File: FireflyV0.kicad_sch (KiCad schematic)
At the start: 18 parts, among them J1 USB4125-GF-A-0190, J2 USB4125-GF-A-0190, J3 USB4125-GF-A-0190, J4 Conn_01x04, J5 Conn_01x03, U1 PEC12R-4215F-S0024, U2 Pico

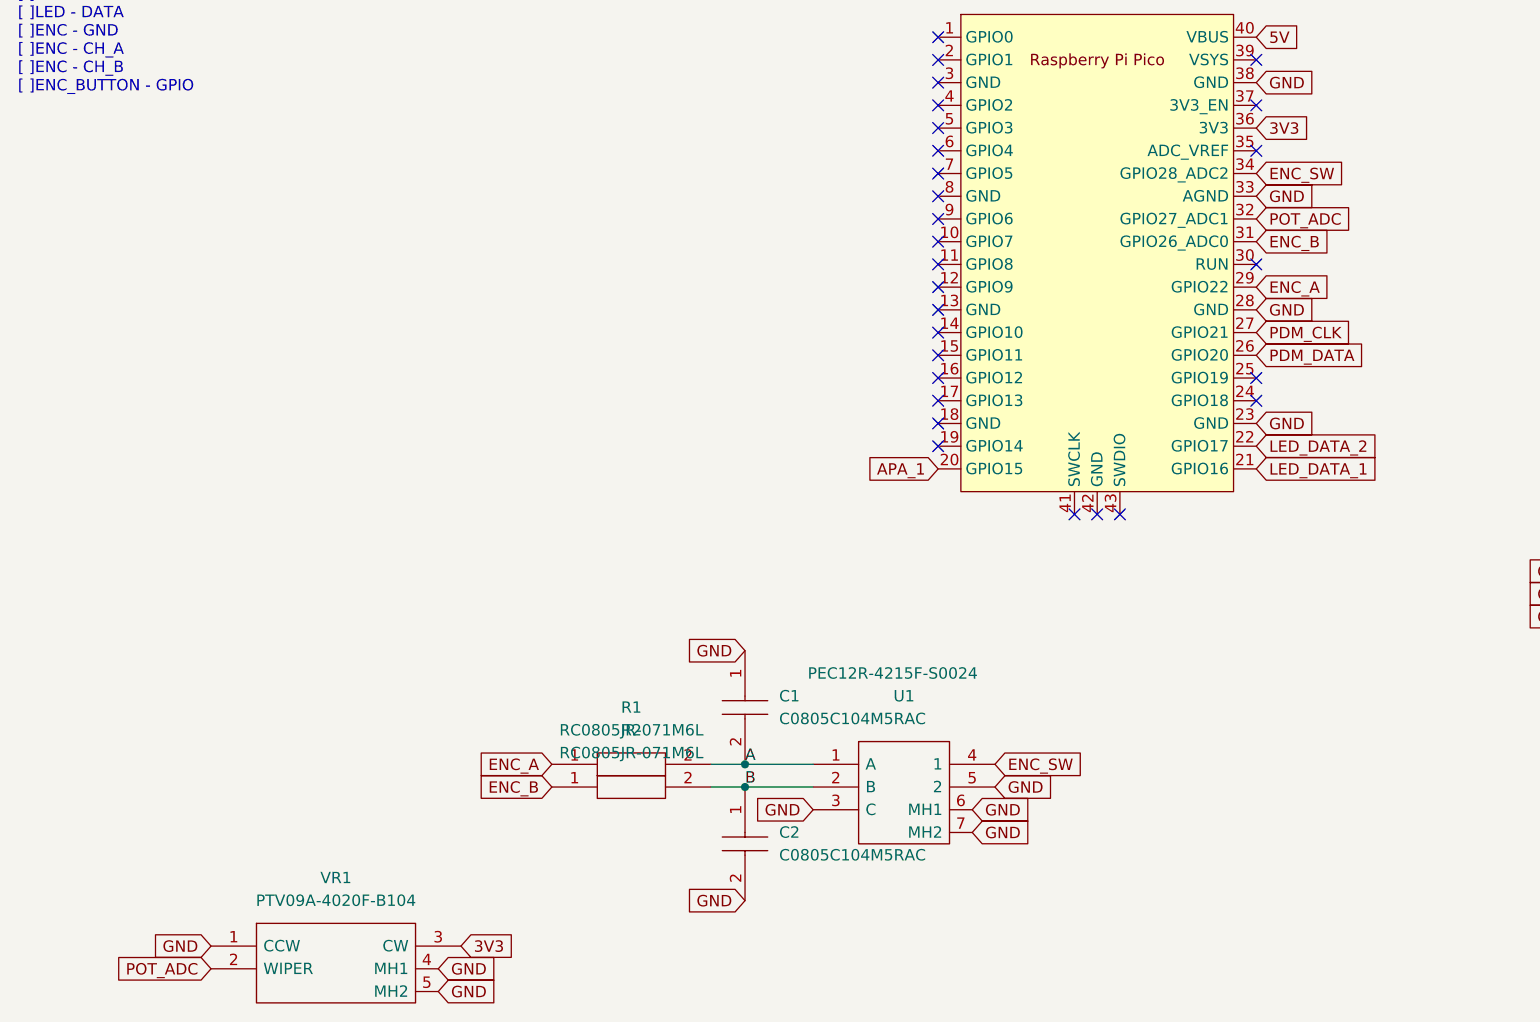
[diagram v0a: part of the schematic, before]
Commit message: Adding puttons
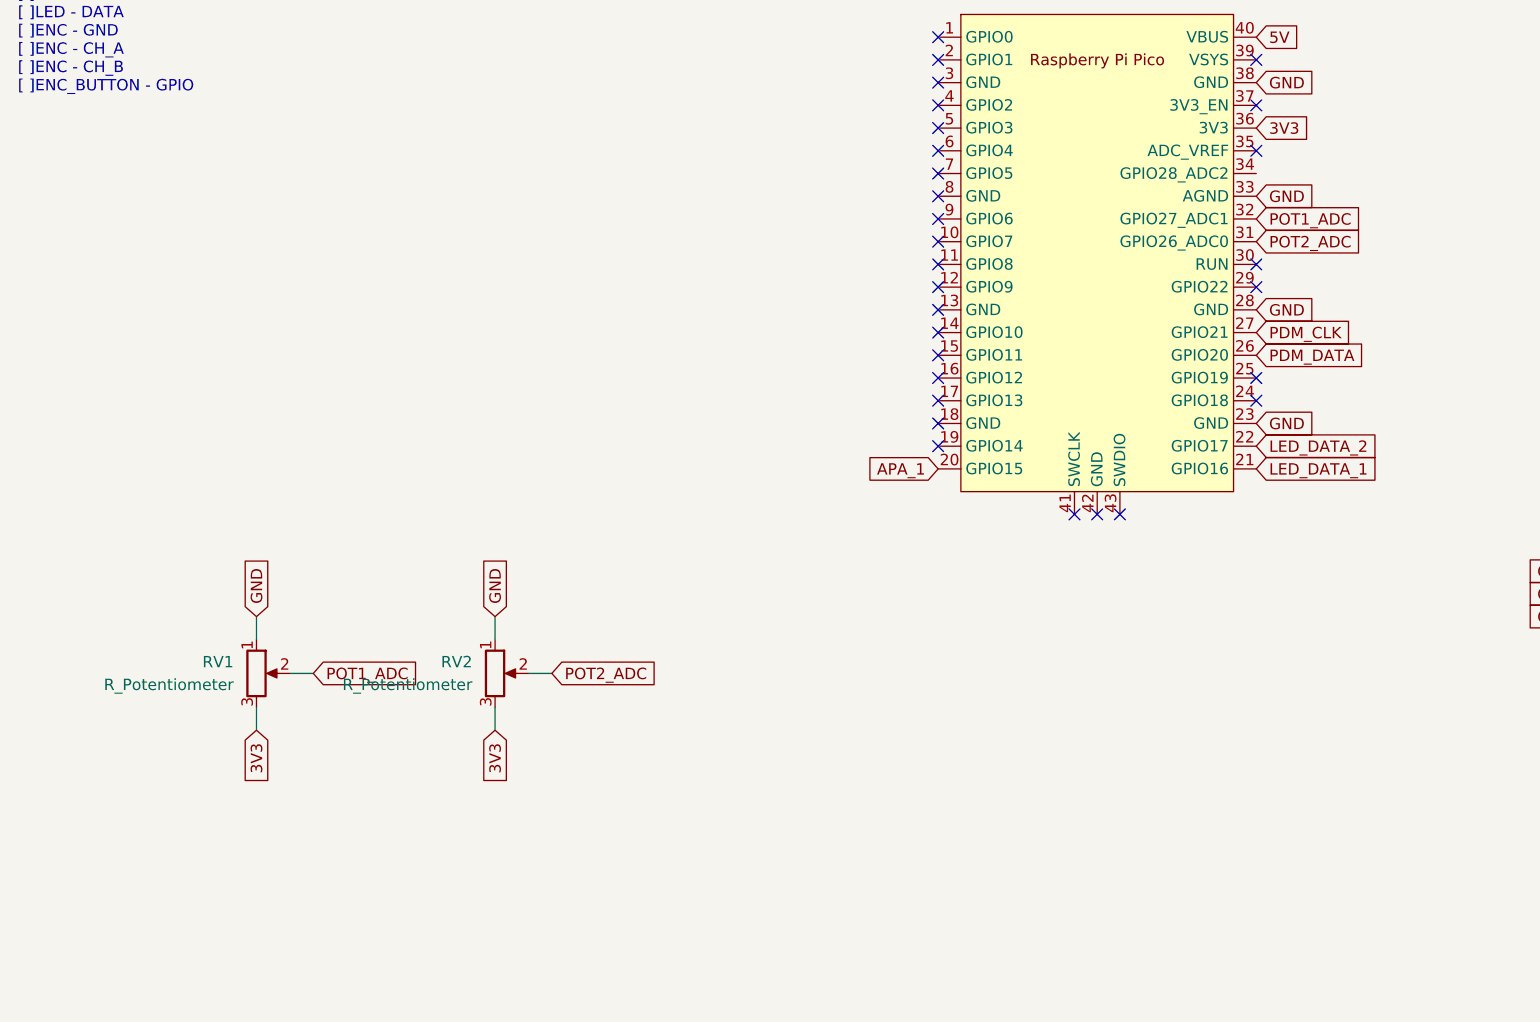
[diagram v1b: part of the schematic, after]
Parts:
- removed C1, C2: C0805C104M5RAC, SamacSys_Parts:CAPC2012X88N, symbol SamacSys_Parts:C0805C104M5RAC
- removed R1, R2: RC0805JR-071M6L, SamacSys_Parts:RESC2012X60N, symbol SamacSys_Parts:RC0805JR-071M6L
- removed U1: PEC12R-4215F-S0024, SamacSys_Parts:PEC12R-4XXXF-SXXXX_court, symbol SamacSys_Parts:PEC12R-4215F-S0024
- removed VR1: PTV09A-4020F-B104, SamacSys_Parts:PTV09A4020FB103, symbol SamacSys_Parts:PTV09A-4020F-B104
- added RV1, RV2: R_Potentiometer, Varistor:3352T-1-104LF, symbol Device:R_Potentiometer
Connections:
- net 3V3: now also RV1.3, RV2.3
- net GND: now also RV1.1, RV2.1
- net ENC_A: no longer names the net of U2.29 (GPIO22)
- net ENC_B renamed POT2_ADC
- net POT2_ADC: now also RV2.2
- net ENC_SW: no longer names the net of U2.34 (GPIO28_ADC2)
- net POT_ADC renamed POT1_ADC
- net POT1_ADC: now also RV1.2
- no-connect marks 34 -> 35
